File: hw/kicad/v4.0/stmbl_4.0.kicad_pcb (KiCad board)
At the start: 2 copper layers, 100 x 100 mm, 433 parts, among them J1 RJ45_LED, J2 RJ45_LED, J3 RJ45_LED, P1 USB_OTG, P10 CONN_02X06, P11 USB_OTG, P12 CONN_01X04, P13 CONN_01X04, P14 CONN_01X04, P15 CONN_01X02, P2 CONN_01X02, P3 CONN_01X02, P4 CONN_01X02, P5 CONN_01X06, P6 CONN_01X02, P7 CONN_01X04, P8 CONN_01X03, P9 CONN_01X06, Q1 IRLML6344, Q2 IRLML6344, Q3 IRLML6344, Q4 IRLML6344, Q5 IRLML6344, T1 testpoint, T2 testpoint, T44 testpoint, T45 testpoint, T46 testpoint, U1 USBLC6-4SC6, U10 SN65176B, U11 SN65176B, U12 IRAM256a, U13 ACT4088, U14 SN65176B, U15 SN65176B, U16 SN65176B, U17 SN65176B, U18 SN65176B, U19 SN65176B, U2 zldo1117, U20 USBLC6-4SC6, U21 USBLC6-4SC6, U22 USBLC6-4SC6, U23 USBLC6-4SC6, U24 non_plated, U25 STM32F303CBTx, U26 STM32F405VG, U27 ACT4088, U28 ACT4088, U29 USBLC6-4SC6, U3 SI8621, U30 non_plated, U31 non_plated, U32 non_plated, U33 heatsink, U34 fan, U35 non_plated, U36 non_plated, U37 non_plated, U39 non_plated, U4 ACT4088, U5 LNK304D, U6 LM358, U7 LM358, U8 SN65176B, U9 SN65176B, Y1 8M, Y2 8M

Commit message: added HW files
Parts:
- added C146: EKMG500ELL470MF11D, SamacSys_Parts:CAPPRD250W60D680H1250, F.Cu at (125.2, 118.2)
- added C148: EKMG500ELL470MF11D, SamacSys_Parts:CAPPRD250W60D680H1250, F.Cu at (132.5, 117.8)
- added C149: EKMG500ELL470MF11D, SamacSys_Parts:CAPPRD250W60D680H1250, F.Cu at (142.8, 115.2)
- added U24: non_plated, stmbl:non_plated_3mm, B.Cu at (117.0, 136.8)
- added U31: non_plated, stmbl:non_plated_3mm, B.Cu at (177.0, 136.8)
- added U36: non_plated, stmbl:non_plated_1mm, F.Cu at (182.0, 102.0)
- added U36: non_plated, stmbl:non_plated_1mm, F.Cu at (114.5, 101.8)
- C20, C33, C45: moved to B.Cu
- C42, C43, C44: footprint stmbl:C_0603 -> stmbl:C_1206
- moved C23 1.68 mm to (172.8, 130.5), turned to 180 degrees
- moved C20 1.50 mm to (175.5, 129.8), turned to 90 degrees
- moved C33 1.50 mm to (176.8, 129.8), turned to 90 degrees
- moved C45 1.50 mm to (178.0, 129.8), turned to 90 degrees
- moved C42 1.12 mm to (128.2, 117.2)
- moved C44 0.90 mm to (138.5, 117.2)
- moved C43 0.79 mm to (133.5, 117.5)
- moved U33 0.71 mm to (113.0, 104.2)
- moved U34 0.71 mm to (114.5, 104.2)
- moved U35 0.56 mm to (181.8, 104.8)
- moved U39 0.56 mm to (183.2, 104.8)
- moved U12 0.25 mm to (147.0, 137.0)
- moved U36 0.25 mm to (113.0, 101.8)
- moved U37 0.25 mm to (183.5, 102.0)
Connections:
- P1 pad 1: (no net) -> Net-(P1-Pad1)
- P1 pad 4: (no net) -> Net-(P1-Pad4)
- P11 pad 1: (no net) -> Net-(P11-Pad1)
- P11 pad 4: (no net) -> Net-(P11-Pad4)
- U1 pad 4: (no net) -> Net-(U1-Pad4)
- U1 pad 6: (no net) -> Net-(U1-Pad6)
- U13 pad 3: (no net) -> Net-(U13-Pad3)
- U21 pad 4: (no net) -> Net-(U21-Pad4)
- U27 pad 3: (no net) -> Net-(U27-Pad3)
- U4 pad 3: (no net) -> Net-(U4-Pad3)
- U7 pad 8: Net-(C37-Pad2) -> Net-(U7-Pad8)
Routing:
- net /hv/f3/A_HV: track 27.1 -> 39.9 mm
- net /hv/back-emf/W: track 8.68 -> 16.9 mm
- net /hv/f3/A_T_MOT: track 79.2 -> 86.9 mm
- net Net-(C149-Pad2): track 1.75 -> 6.71 mm
- net /hv/back-emf/V: track 8.68 -> 13.5 mm
- net Net-(C146-Pad2): track 1.71 -> 6.17 mm
- net /hv/f3/A_U: track 55.8 -> 58.5 mm, vias 2 -> 4
- net /hv/back-emf/U: track 8.68 -> 10.9 mm
- net Net-(C148-Pad2): track 1.72 -> 3.71 mm
- net /hv/cur/A_IV: track 17.3 -> 18.6 mm, vias 2 -> 3
- net /hv/f3/A_V: track 49.3 -> 48.1 mm
- net /hv/f3/A_W: track 53.3 -> 52.2 mm
- net /hv/f3/BRK: track 62.8 -> 61.9 mm
- net /hv/cur/A_IU: track 15.4 -> 16.2 mm, vias 2 -> 3
- net GNDPWR: vias 130 -> 125
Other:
- outline, holes or cut-outs redrawn

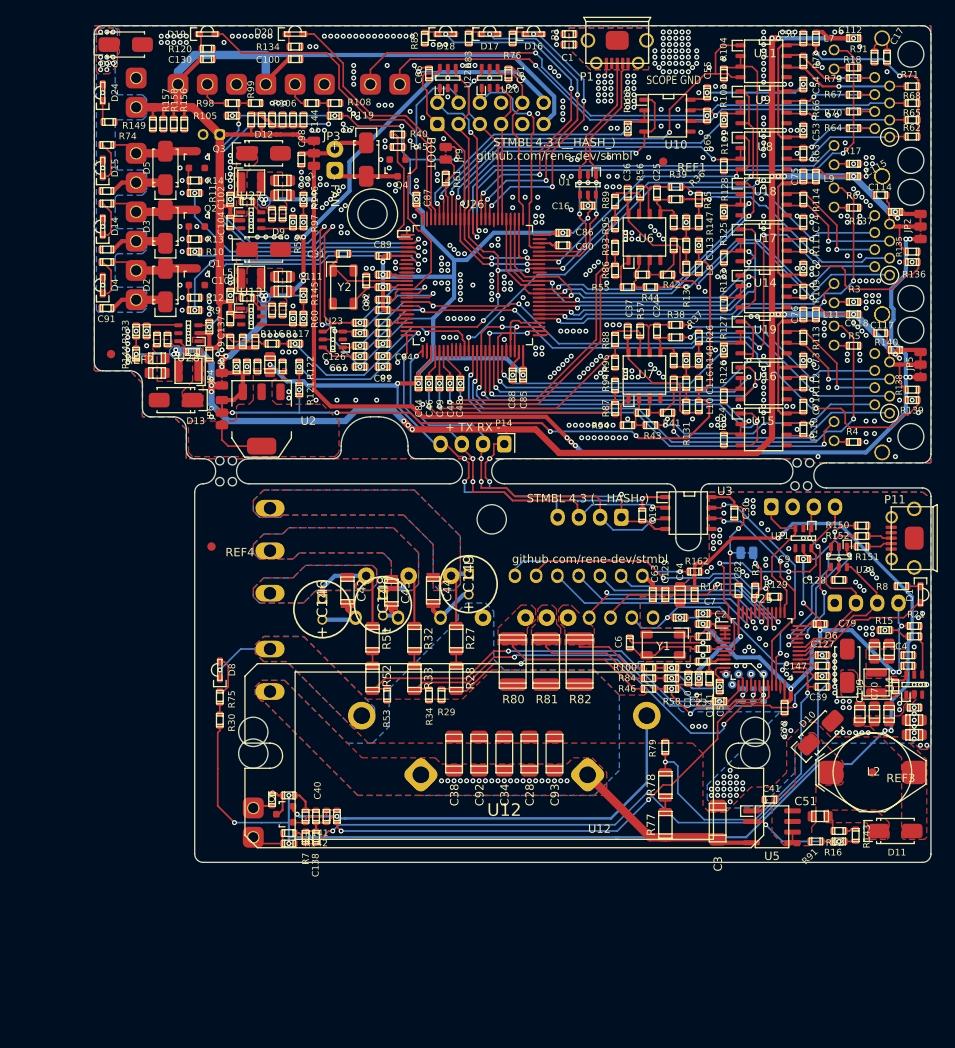
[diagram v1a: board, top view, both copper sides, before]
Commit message: added IKCM30F60GD
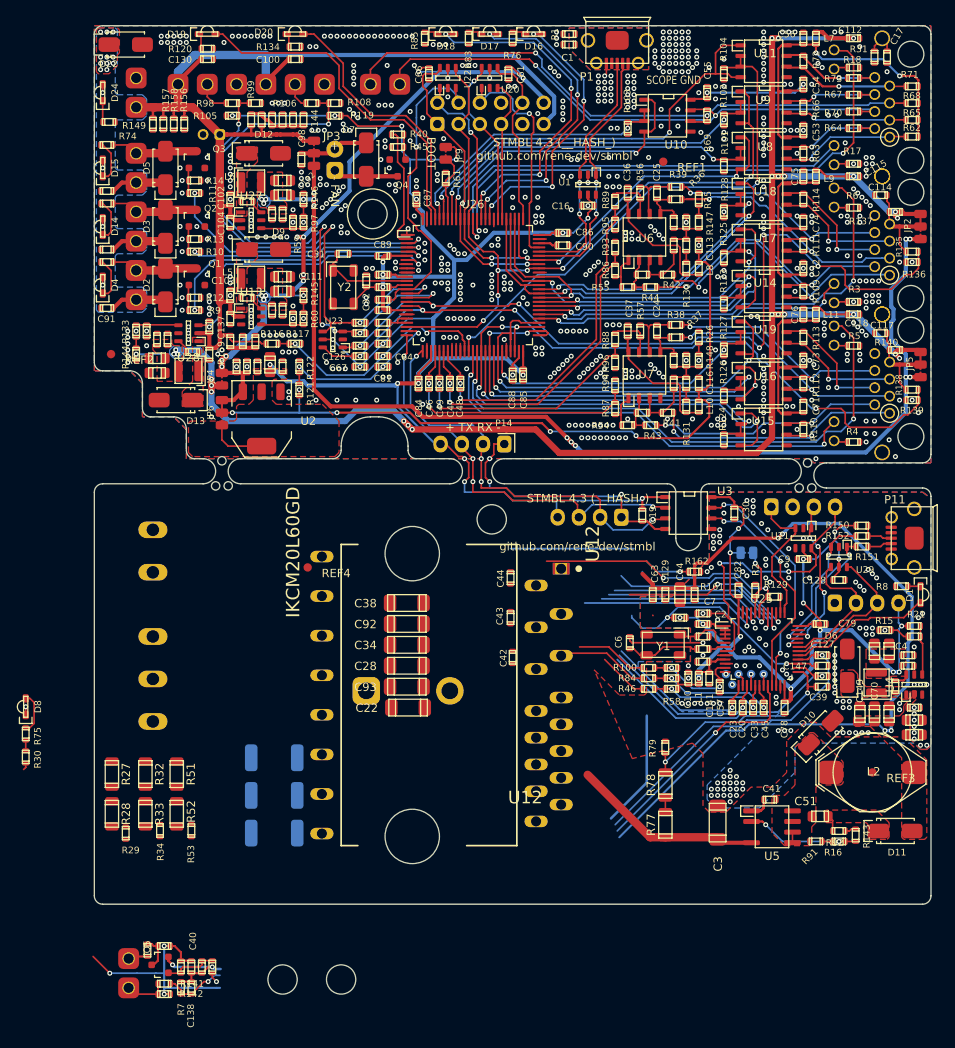
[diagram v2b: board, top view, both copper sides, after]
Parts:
- removed C146, C148, C149: EKMG500ELL470MF11D, SamacSys_Parts:CAPPRD250W60D680H1250
- removed the U24 at (117.0, 136.8)
- removed the U31 at (177.0, 136.8)
- removed the U36 at (182.0, 102.0)
- removed the U36 at (114.5, 101.8)
- C20, C33, C45: moved to F.Cu
- C22: value 270µ -> 150n; footprint stmbl:C_Radial_D26_L45_P10 -> stmbl:C_1808; moved to F.Cu
- C42, C43, C44: footprint stmbl:C_1206 -> stmbl:C_0603
- R80, R81, R82: moved to B.Cu
- U12: value IRAM256a -> IKCM20L60GD; footprint stmbl:IRAM256 -> stmbl:INF-CIPOS_MINI
- moved U31 56.4 mm to (127.5, 163.8)
- moved LOGO1 52.3 mm to (196.0, 163.1)
- moved R27 44.2 mm to (100.1, 139.2)
- moved R28 44.2 mm to (100.1, 143.9)
- moved R82 41.9 mm to (119.5, 146.2), turned to 180 degrees
- moved REF** 41.5 mm to (94.8, 102.2)
- moved R29 41.2 mm to (101.8, 146.2)
- moved R81 36.2 mm to (119.5, 141.8), turned to 180 degrees
- moved R32 36.0 mm to (104.1, 139.2)
- moved R33 36.0 mm to (104.1, 143.9)
- moved R34 36.0 mm to (105.8, 145.9)
- moved R80 30.7 mm to (119.5, 137.2), turned to 180 degrees
- moved R51 28.5 mm to (107.8, 139.2)
- moved R52 28.5 mm to (107.8, 143.9)
- moved R53 28.5 mm to (109.6, 145.9)
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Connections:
- C42 pad 1: /hv/back-emf/W -> Net-(C42-Pad1)
- C42 pad 2: Net-(C146-Pad2) -> Net-(C42-Pad2)
- C43 pad 1: /hv/back-emf/V -> Net-(C43-Pad1)
- C43 pad 2: Net-(C148-Pad2) -> Net-(C43-Pad2)
- C44 pad 1: /hv/back-emf/U -> Net-(C44-Pad1)
- C44 pad 2: Net-(C149-Pad2) -> Net-(C44-Pad2)
- U12 pad 1: Net-(C146-Pad2) -> Net-(C44-Pad1)
- U12 pad 10: /hv/back-emf/U -> /hv/driver/LU
- U12 pad 13: VPP -> +15V
- U12 pad 16: /hv/driver/itirp -> GNDPWR
- U12 pad 17: /hv/driver/CUH -> /hv/driver/CWH
- U12 pad 18: /hv/f3/HV_EN -> /hv/driver/CVH
- U12 pad 19: /hv/driver/CVH -> /hv/driver/CUH
- U12 pad 2: /hv/back-emf/W -> Net-(C44-Pad2)
- U12 pad 20: /hv/driver/HU -> /hv/back-emf/W
- U12 pad 21: /hv/driver/CWH -> /hv/back-emf/V
- U12 pad 22: /hv/driver/HV -> /hv/back-emf/U
- U12 pad 23: /hv/driver/HW -> VPP
- U12 pad 24: /hv/driver/LU -> (no net)
- U12 pad 5: Net-(C148-Pad2) -> Net-(C42-Pad1)
- U12 pad 6: /hv/back-emf/V -> Net-(C42-Pad2)
- U12 pad 9: Net-(C149-Pad2) -> /hv/driver/HW
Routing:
- net +15V: track 169.0 -> 127.5 mm
- net /hv/f3/A_T_MOT: track 86.9 -> 46.9 mm
- net GNDPWR: track 84.0 -> 44.3 mm, vias 125 -> 130
- net /hv/f3/A_W: track 52.2 -> 19.2 mm, vias 2 -> 1
- net /hv/f3/BRK: track 61.9 -> 29.8 mm
- net /hv/f3/A_V: track 48.1 -> 20.8 mm, vias 2 -> 1
- net /hv/f3/A_U: track 58.5 -> 32.8 mm, vias 4 -> 1
- net /hv/back-emf/W: track 16.9 -> 0.00 mm
- net /hv/back-emf/V: track 13.5 -> 0.00 mm
- net /hv/driver/CUH: track 18.8 -> 5.90 mm
- net /hv/f3/A_HV: track 39.9 -> 27.1 mm
- net /hv/back-emf/U: track 10.9 -> 0.00 mm
- net Net-(C149-Pad2): track 6.71 -> 0.00 mm
- net Net-(C146-Pad2): track 6.17 -> 0.00 mm
- net /hv/driver/HU: track 27.4 -> 22.3 mm
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- removed copper zone on B.Cu, net /hv/back-emf/U
- removed copper zone on F.Cu, net /hv/back-emf/U
- removed copper zone on B.Cu, net /hv/back-emf/V
- removed copper zone on F.Cu, net /hv/back-emf/V
- removed copper zone on B.Cu, net /hv/back-emf/W
- removed copper zone on F.Cu, net /hv/back-emf/W
- removed copper zone on F.Cu, net /hv/driver/CUH
- removed copper zone on F.Cu, net /hv/driver/CVH
- removed copper zone on F.Cu, net /hv/driver/CWH
- removed copper zone on B.Cu, net VPP
- removed copper zone on F.Cu, net VPP
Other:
- board size 100 x 100 mm -> 100 x 105 mm
- board text removed: "+ +"
- board text removed: "- -"
- board text removed: "- TH LV HW W- V- U- + UB VB WB"
- board text removed: "15V LW LU HV HU EN iT U V W"
- board text removed: "C21"
- board text removed: "C22"

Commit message: changes for IKCM30F60GD
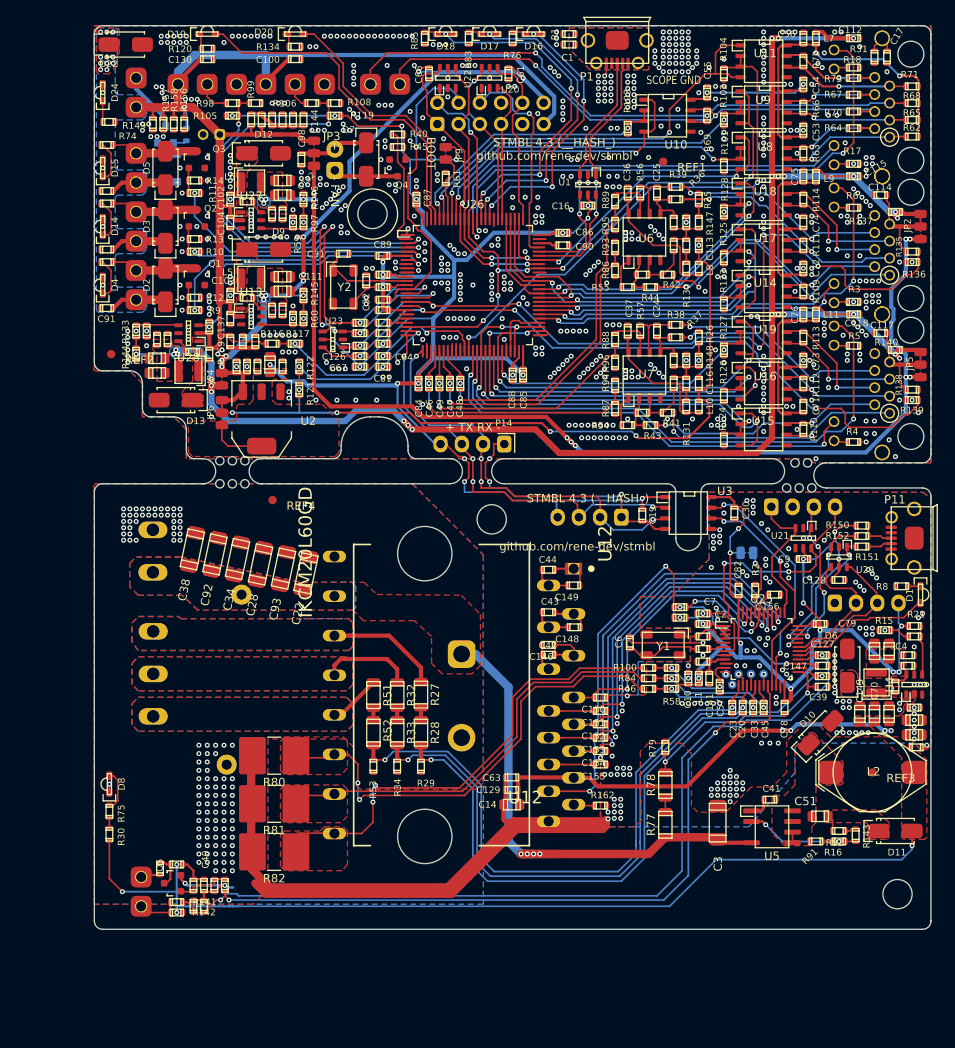
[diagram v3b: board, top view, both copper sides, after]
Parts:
- removed U24: non_plated, stmbl:non_plated_3mm
- added C146: 100n, stmbl:C_0603, F.Cu at (152.2, 123.8)
- added C148: 100n, stmbl:C_0603, F.Cu at (155.3, 121.7)
- added C149: 100n, stmbl:C_0603, F.Cu at (155.3, 116.7)
- added C150: 1n, stmbl:C_0603, F.Cu at (158.5, 130.1)
- added C151: 1n, stmbl:C_0603, F.Cu at (158.5, 131.7)
- added C152: 1n, stmbl:C_0603, F.Cu at (158.5, 133.2)
- added C153: 1n, stmbl:C_0603, F.Cu at (158.5, 134.8)
- added C154: 1n, stmbl:C_0603, F.Cu at (158.5, 136.4)
- added C155: 1n, stmbl:C_0603, F.Cu at (158.5, 138.1)
- added C156: 10n, stmbl:C_0603, F.Cu at (179.3, 117.8)
- added C157: 150n, stmbl:C_Rect_L24.0mm_W10.1mm_P22.50mm_MKT, B.Cu at (115.7, 116.9)
- added D21: BZT52Bxx, Diode_SMD:D_SOD-123, B.Cu at (107.8, 66.8)
- added Q6: AO3400A, Package_TO_SOT_SMD:SOT-23, B.Cu at (106.5, 62.8)
- added R168: 1k, stmbl:R_0603, F.Cu at (168.0, 119.2)
- added U37: non_plated, stmbl:non_plated_1mm, F.Cu at (116.0, 104.5)
- added U37: non_plated, stmbl:non_plated_1mm, F.Cu at (116.0, 101.8)
- added U37: non_plated, stmbl:non_plated_1mm, F.Cu at (114.5, 101.8)
- added U37: non_plated, stmbl:non_plated_1mm, F.Cu at (180.8, 105.0)
- added U37: non_plated, stmbl:non_plated_1mm, F.Cu at (181.8, 102.0)
- R115: value 10k -> 3.9k
- R129: value 1k -> 100k; moved to B.Cu
- R143: value 1.5k -> 3.9k
- R80, R81, R82: footprint stmbl:R_2512 -> Resistor_SMD:R_2816_7142Metric_Pad3.20x4.45mm_HandSolder; moved to F.Cu
- moved R129 89.4 mm to (109.0, 62.8), turned to 270 degrees
- moved U31 67.3 mm to (194.0, 153.6)
- moved R28 38.2 mm to (137.0, 134.2)
- moved R27 38.1 mm to (137.0, 129.7)
- moved R29 36.2 mm to (137.0, 138.2)
- moved REF** 36.0 mm to (130.0, 109.8)
- moved R161 32.2 mm to (196.2, 136.0), turned to 0 degrees
- moved C14 32.2 mm to (147.9, 142.8), turned to 0 degrees
- moved R33 31.6 mm to (134.2, 134.2)
- moved R32 31.5 mm to (134.2, 129.8)
- moved R162 30.1 mm to (158.5, 143.0)
- moved C129 29.7 mm to (147.9, 141.1), turned to 180 degrees
- moved R34 29.4 mm to (134.2, 138.2)
- moved C63 27.6 mm to (147.9, 139.6), turned to 180 degrees
- moved C38 26.4 mm to (109.7, 112.3), turned to 78 degrees
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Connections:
- P3 pad 2: GND -> Net-(P3-Pad2)
- R129 pad 1: /hv/f3/HV_EN -> +24V
- R129 pad 2: Net-(R129-Pad2) -> Net-(D21-Pad1)
- U25 pad 38: Net-(R129-Pad2) -> Net-(U25-Pad38)
- U25 pad 43: /hv/f3/HV_EN -> /hv/f3/HV_FLT
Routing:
- net GNDPWR: track 44.3 -> 146.3 mm, vias 130 -> 259
- net /hv/f3/BRK: track 29.8 -> 87.8 mm
- net /hv/f3/A_T_MOT: track 46.9 -> 104.1 mm
- net /hv/f3/A_W: track 19.2 -> 73.4 mm, vias 1 -> 2
- net /hv/driver/CUH: track 5.90 -> 57.6 mm, vias 0 -> 2
- net /hv/f3/A_V: track 20.8 -> 71.7 mm, vias 1 -> 2
- net /hv/f3/A_U: track 32.8 -> 80.6 mm, vias 1 -> 2
- net /hv/driver/CWH: track 8.49 -> 54.8 mm, vias 0 -> 2
- net +15V: track 127.5 -> 170.4 mm, vias 7 -> 8
- net /hv/driver/CVH: track 11.9 -> 51.2 mm
- net VPP: track 22.9 -> 62.1 mm, vias 0 -> 4
- net /hv/f3/A_T_HV: track 27.8 -> 62.4 mm, vias 2 -> 4
- net /hv/f3/HV_EN: track 31.3 -> 0.00 mm, vias 2 -> 0
- net /hv/driver/LW: track 23.1 -> 49.3 mm, vias 1 -> 2
- net /hv/driver/LV: track 22.4 -> 45.7 mm
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- added copper zone on B.Cu, net /hv/back-emf/U
- added copper zone on F.Cu, net /hv/back-emf/U
- added copper zone on B.Cu, net /hv/back-emf/V
- added copper zone on F.Cu, net /hv/back-emf/V
- added copper zone on B.Cu, net /hv/back-emf/W
- added copper zone on F.Cu, net /hv/back-emf/W
- added copper zone on F.Cu, net /hv/driver/CUH
- added copper zone on F.Cu, net /hv/driver/CVH
- added copper zone on F.Cu, net /hv/driver/CWH
- added copper zone on B.Cu, net VPP
- added copper zone on F.Cu, net VPP
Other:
- board size 100 x 105 mm -> 100 x 108 mm
- net class UVW: clearance 0.5 -> 0.75
- net class UVW_L: clearance 0.2 -> 0.5
